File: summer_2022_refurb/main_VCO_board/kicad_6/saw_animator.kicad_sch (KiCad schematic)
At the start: 23 parts, among them U6 TL074, U7 LM311

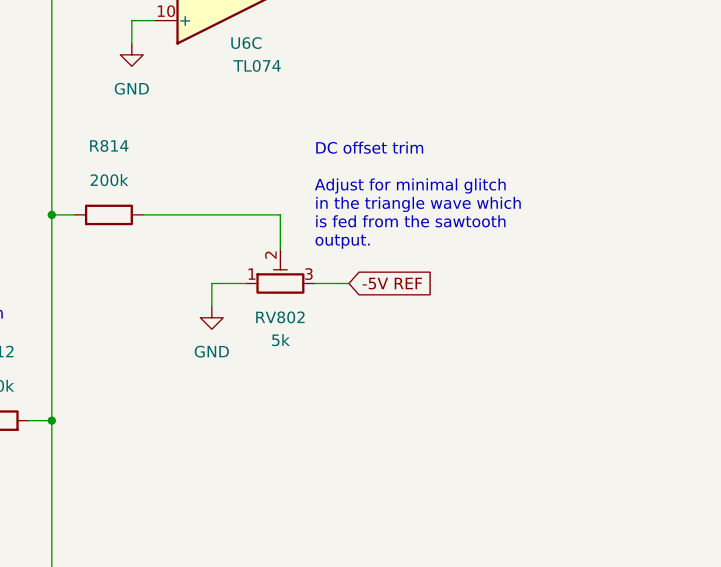
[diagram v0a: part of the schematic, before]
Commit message: Fix VCO issues, suboct switching, component values
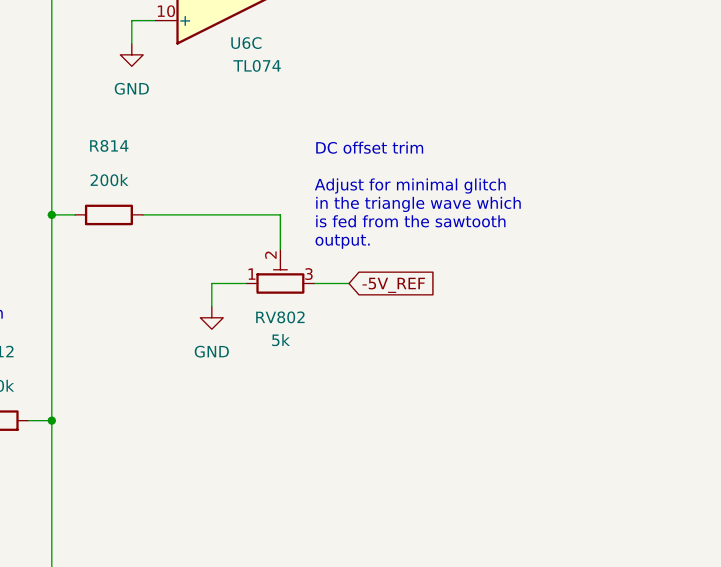
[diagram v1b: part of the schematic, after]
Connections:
- net -5V REF renamed -5V_REF
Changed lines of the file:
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@@
   (title_block
     (title "Josh Ox Ribon Synth Main VCO board")
-    (date "2022-06-18")
-    (rev "0")
+    (date "2022-07-07")
+    (rev "0.1")
     (comment 2 "creativecommons.org/licences/by/4.0")
     (comment 3 "license: CC by 4.0")
@@
     (effects (font (size 1.27 1.27)) (justify left bottom))
   )
-  (global_label "-5V REF" (shape input) (at 241.3 81.28 0) (fields_autoplaced)
+  (global_label "-5V_REF" (shape input) (at 241.3 81.28 0) (fields_autoplaced)
     (effects (font (size 1.27 1.27)) (justify left))
     (property "Intersheet References" "${INTERSHEET_REFS}" (id 0) (at 252.0588 81.2006 0)
